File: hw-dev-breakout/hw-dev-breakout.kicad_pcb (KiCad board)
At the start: 2 copper layers, 70 x 57.5 mm, 5 parts, among them J1 CN7, J2 CN10

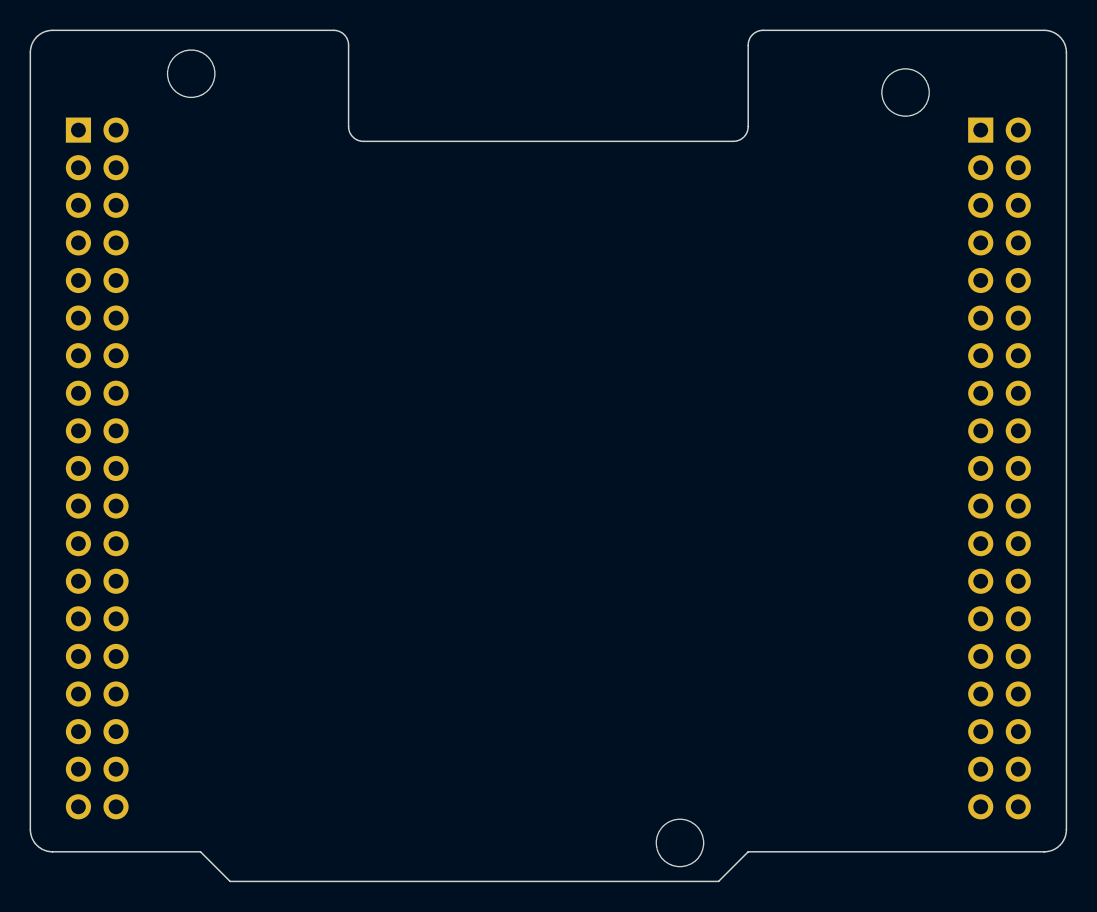
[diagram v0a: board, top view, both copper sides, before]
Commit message: pcb: Move the Nucleo outline onto a comment layout
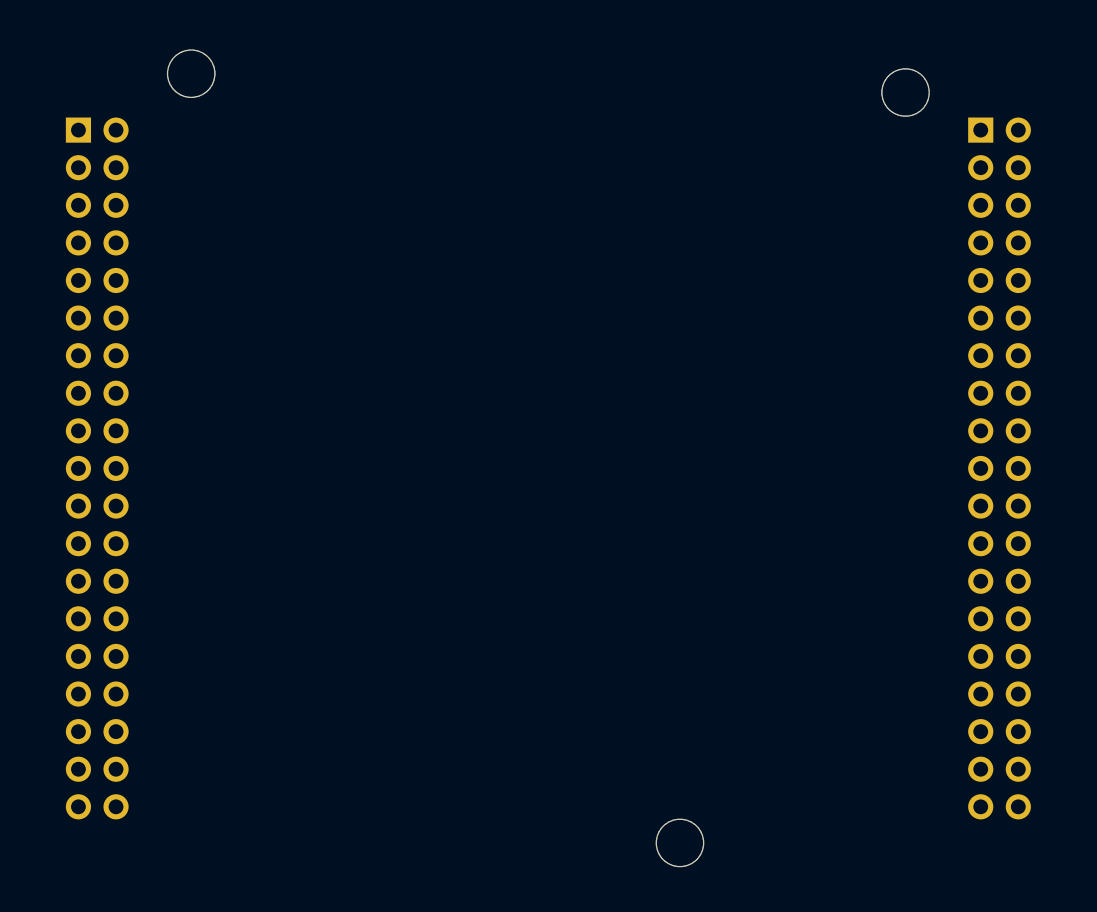
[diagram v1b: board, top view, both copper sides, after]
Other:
- board outline removed
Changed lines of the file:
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@@
 			(type solid)
 		)
-		(layer "Edge.Cuts")
+		(layer "Cmts.User")
 	)
 	(gr_line
@@
 			(type solid)
 		)
-		(layer "Edge.Cuts")
+		(layer "Cmts.User")
 	)
 	(gr_arc
@@
 			(type solid)
 		)
-		(layer "Edge.Cuts")
+		(layer "Cmts.User")
 	)
 	(gr_line
@@
 			(type solid)
 		)
-		(layer "Edge.Cuts")
+		(layer "Cmts.User")
 	)
 	(gr_arc
@@
 			(type solid)
 		)
-		(layer "Edge.Cuts")
+		(layer "Cmts.User")
 	)
 	(gr_arc
@@
 			(type solid)
 		)
-		(layer "Edge.Cuts")
+		(layer "Cmts.User")
 	)
 	(gr_arc
@@
 			(type solid)
 		)
-		(layer "Edge.Cuts")
+		(layer "Cmts.User")
 	)
 	(gr_arc
@@
 			(type solid)
 		)
-		(layer "Edge.Cuts")
+		(layer "Cmts.User")
 	)
 	(gr_line
@@
 			(type solid)
 		)
-		(layer "Edge.Cuts")
+		(layer "Cmts.User")
 	)
 	(gr_arc
@@
 			(type solid)
 		)
-		(layer "Edge.Cuts")
+		(layer "Cmts.User")
 	)
 	(gr_line
@@
 			(type solid)
 		)
-		(layer "Edge.Cuts")
+		(layer "Cmts.User")
 	)
 	(gr_line
@@
 			(type solid)
 		)
-		(layer "Edge.Cuts")
+		(layer "Cmts.User")
 	)
 	(gr_arc
@@
 			(type solid)
 		)
-		(layer "Edge.Cuts")
+		(layer "Cmts.User")
 	)
 	(gr_line
@@
 			(type solid)
 		)
-		(layer "Edge.Cuts")
+		(layer "Cmts.User")
 	)
 	(gr_arc
@@
 			(type solid)
 		)
-		(layer "Edge.Cuts")
+		(layer "Cmts.User")
 	)
 	(gr_line
@@
 			(type solid)
 		)
-		(layer "Edge.Cuts")
+		(layer "Cmts.User")
 	)
 	(gr_line
@@
 			(type solid)
 		)
-		(layer "Edge.Cuts")
+		(layer "Cmts.User")
 	)
 	(gr_line
@@
 			(type solid)
 		)
-		(layer "Edge.Cuts")
+		(layer "Cmts.User")
 	)
 	(gr_line
@@
 			(type solid)
 		)
-		(layer "Edge.Cuts")
+		(layer "Cmts.User")
 	)
 	(gr_line
@@
 			(type solid)
 		)
-		(layer "Edge.Cuts")
+		(layer "Cmts.User")
 	)
 )

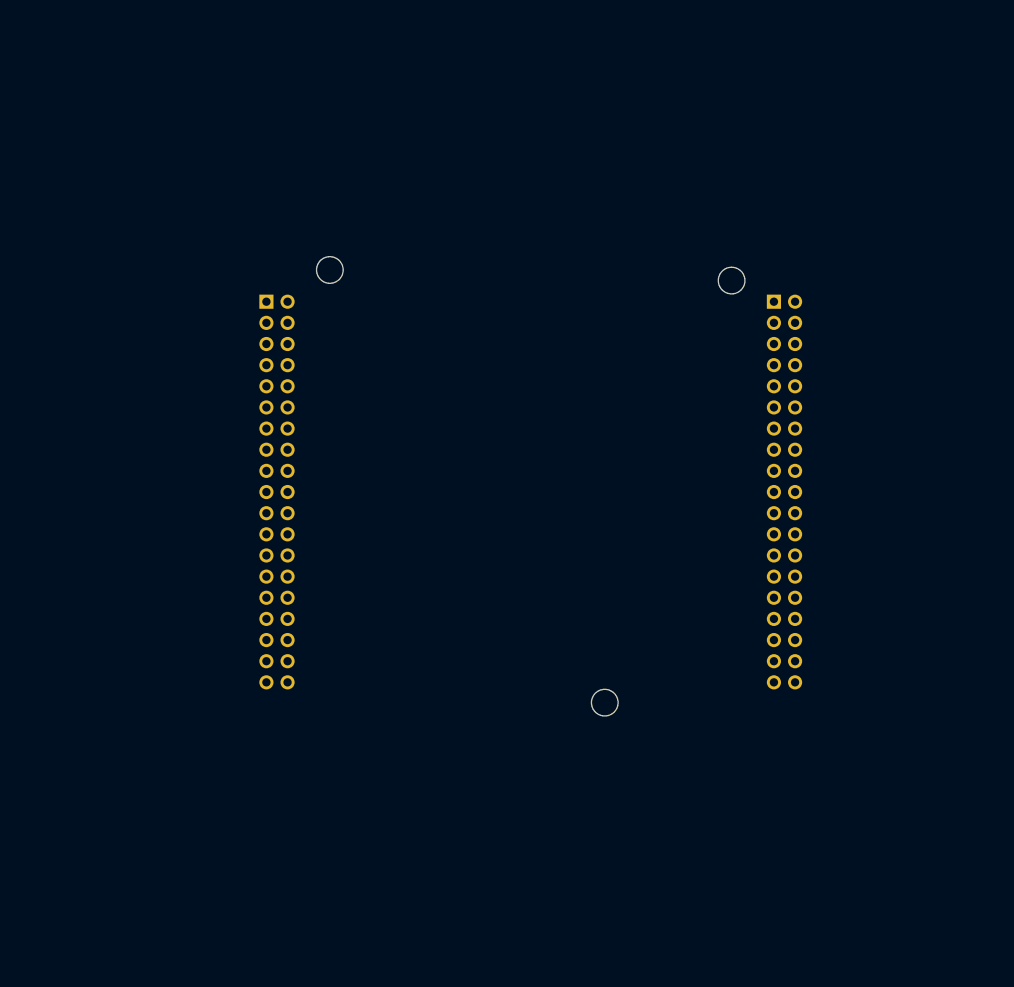
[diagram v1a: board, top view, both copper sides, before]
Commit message: pcb: Initial components placed
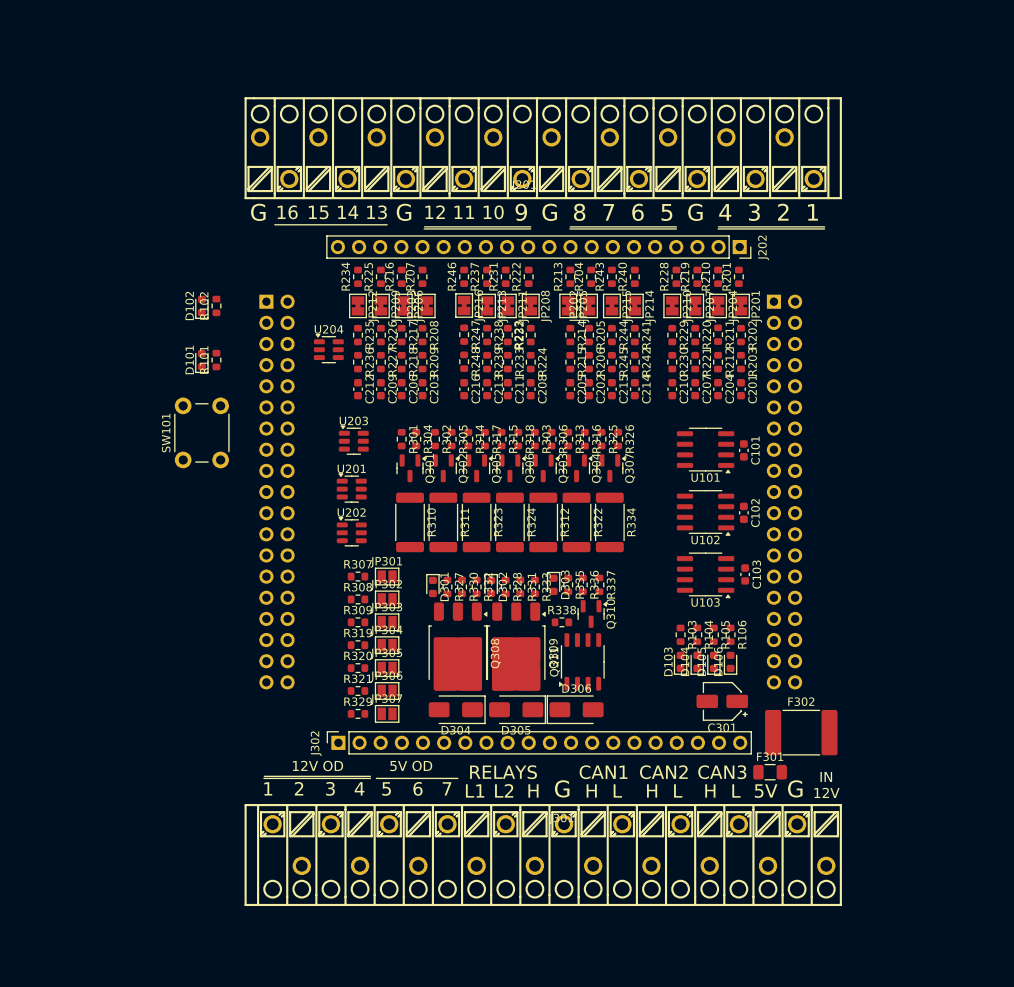
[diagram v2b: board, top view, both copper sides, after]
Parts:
- removed H1, H2, H3: MountingHole, MountingHole:MountingHole_3.2mm_M3
- added C101: 100nF, Capacitor_SMD:C_0603_1608Metric, F.Cu at (162.1, 80.1)
- added C102: 100nF, Capacitor_SMD:C_0603_1608Metric, F.Cu at (162.1, 87.6)
- added C103: 100nF, Capacitor_SMD:C_0603_1608Metric, F.Cu at (162.2, 95.0)
- added C201: DNP, Capacitor_SMD:C_0603_1608Metric, F.Cu at (161.8, 72.8)
- added C202: DNP, Capacitor_SMD:C_0603_1608Metric, F.Cu at (143.5, 72.8)
- added C203: DNP, Capacitor_SMD:C_0603_1608Metric, F.Cu at (123.5, 72.8)
- added C204: DNP, Capacitor_SMD:C_0603_1608Metric, F.Cu at (159.0, 72.8)
- added C205: DNP, Capacitor_SMD:C_0603_1608Metric, F.Cu at (141.2, 72.8)
- added C206: DNP, Capacitor_SMD:C_0603_1608Metric, F.Cu at (121.0, 72.8)
- added C207: DNP, Capacitor_SMD:C_0603_1608Metric, F.Cu at (156.2, 72.8)
- added C208: DNP, Capacitor_SMD:C_0603_1608Metric, F.Cu at (136.5, 72.8)
- added C209: DNP, Capacitor_SMD:C_0603_1608Metric, F.Cu at (118.5, 72.8)
- added C210: DNP, Capacitor_SMD:C_0603_1608Metric, F.Cu at (153.5, 72.8)
- added C211: DNP, Capacitor_SMD:C_0603_1608Metric, F.Cu at (133.8, 72.8)
- added C212: DNP, Capacitor_SMD:C_0603_1608Metric, F.Cu at (115.8, 72.8)
- added C213: DNP, Capacitor_SMD:C_0603_1608Metric, F.Cu at (131.2, 72.8)
- added C214: DNP, Capacitor_SMD:C_0603_1608Metric, F.Cu at (149.0, 72.8)
- added C215: DNP, Capacitor_SMD:C_0603_1608Metric, F.Cu at (146.2, 72.8)
- added C216: DNP, Capacitor_SMD:C_0603_1608Metric, F.Cu at (128.5, 72.8)
- added C301: 10uF 25V, Capacitor_SMD:CP_Elec_4x4.5, F.Cu at (159.5, 110.2)
- added D101: RED, LED_SMD:LED_0603_1608Metric, F.Cu at (97.0, 69.2)
- added D102: RED, LED_SMD:LED_0603_1608Metric, F.Cu at (97.0, 62.8)
- added D103: GREEN, LED_SMD:LED_0603_1608Metric, F.Cu at (154.5, 105.5)
- added D104: GREEN, LED_SMD:LED_0603_1608Metric, F.Cu at (156.5, 105.5)
- added D105: GREEN, LED_SMD:LED_0603_1608Metric, F.Cu at (158.5, 105.5)
- added D106: GREEN, LED_SMD:LED_0603_1608Metric, F.Cu at (160.5, 105.5)
- added D301: ORANGE, LED_SMD:LED_0603_1608Metric, F.Cu at (124.8, 96.5)
- added D302: ORANGE, LED_SMD:LED_0603_1608Metric, F.Cu at (131.8, 96.5)
- added D303: ORANGE, LED_SMD:LED_0603_1608Metric, F.Cu at (139.2, 96.2)
- added D304: SS54, Diode_SMD:D_SMA, F.Cu at (127.5, 111.2)
- added D305: SS54, Diode_SMD:D_SMA, F.Cu at (134.8, 111.2)
- added D306: SS54, Diode_SMD:D_SMA, F.Cu at (142.0, 111.2)
- added F301: 12H1100C 1A, Fuse:Fuse_1206_3216Metric, F.Cu at (165.2, 118.8)
- added F302: LSMD500, Fuse:Fuse_2920_7451Metric, F.Cu at (169.0, 114.0)
- added J201: WAGO 250-220, hw-dev-breakout:CONN-TH_250-220, F.Cu at (137.2, 45.0)
- added J202: Conn_01x16, Connector_PinSocket_2.54mm:PinSocket_1x20_P2.54mm_Vertical, F.Cu at (161.6, 55.7)
- added J301: WAGO 250-220, hw-dev-breakout:CONN-TH_250-220, F.Cu at (138.8, 127.5)
- added J302: Conn_01x20, Connector_PinSocket_2.54mm:PinSocket_1x20_P2.54mm_Vertical, F.Cu at (113.4, 115.2)
- added JP201: SolderJumper_2_Bridged, Jumper:SolderJumper-2_P1.3mm_Bridged_Pad1.0x1.5mm, F.Cu at (161.8, 62.8)
- added JP202: SolderJumper_2_Bridged, Jumper:SolderJumper-2_P1.3mm_Bridged_Pad1.0x1.5mm, F.Cu at (143.5, 62.8)
- added JP203: SolderJumper_2_Bridged, Jumper:SolderJumper-2_P1.3mm_Bridged_Pad1.0x1.5mm, F.Cu at (124.0, 62.8)
- added JP204: SolderJumper_2_Bridged, Jumper:SolderJumper-2_P1.3mm_Bridged_Pad1.0x1.5mm, F.Cu at (159.0, 62.8)
- added JP205: SolderJumper_2_Bridged, Jumper:SolderJumper-2_P1.3mm_Bridged_Pad1.0x1.5mm, F.Cu at (141.0, 62.8)
- added JP206: SolderJumper_2_Bridged, Jumper:SolderJumper-2_P1.3mm_Bridged_Pad1.0x1.5mm, F.Cu at (121.2, 62.8)
- added JP207: SolderJumper_2_Bridged, Jumper:SolderJumper-2_P1.3mm_Bridged_Pad1.0x1.5mm, F.Cu at (156.2, 62.8)
- added JP208: SolderJumper_2_Bridged, Jumper:SolderJumper-2_P1.3mm_Bridged_Pad1.0x1.5mm, F.Cu at (136.5, 62.8)
- added JP209: SolderJumper_2_Bridged, Jumper:SolderJumper-2_P1.3mm_Bridged_Pad1.0x1.5mm, F.Cu at (118.5, 62.8)
- added JP210: SolderJumper_2_Bridged, Jumper:SolderJumper-2_P1.3mm_Bridged_Pad1.0x1.5mm, F.Cu at (153.5, 62.8)
- added JP211: SolderJumper_2_Bridged, Jumper:SolderJumper-2_P1.3mm_Bridged_Pad1.0x1.5mm, F.Cu at (133.8, 62.8)
- added JP212: SolderJumper_2_Bridged, Jumper:SolderJumper-2_P1.3mm_Bridged_Pad1.0x1.5mm, F.Cu at (115.8, 62.8)
- added JP213: SolderJumper_2_Bridged, Jumper:SolderJumper-2_P1.3mm_Bridged_Pad1.0x1.5mm, F.Cu at (131.2, 62.8)
- added JP214: SolderJumper_2_Bridged, Jumper:SolderJumper-2_P1.3mm_Bridged_Pad1.0x1.5mm, F.Cu at (149.0, 62.8)
- added JP215: SolderJumper_2_Bridged, Jumper:SolderJumper-2_P1.3mm_Bridged_Pad1.0x1.5mm, F.Cu at (146.2, 62.8)
- added JP216: SolderJumper_2_Bridged, Jumper:SolderJumper-2_P1.3mm_Bridged_Pad1.0x1.5mm, F.Cu at (128.5, 62.7)
- added JP301: SolderJumper_2_Open, Jumper:SolderJumper-2_P1.3mm_Open_Pad1.0x1.5mm, F.Cu at (119.2, 95.2)
- added JP302: SolderJumper_2_Open, Jumper:SolderJumper-2_P1.3mm_Open_Pad1.0x1.5mm, F.Cu at (119.2, 98.0)
- added JP303: SolderJumper_2_Open, Jumper:SolderJumper-2_P1.3mm_Open_Pad1.0x1.5mm, F.Cu at (119.2, 100.8)
- added JP304: SolderJumper_2_Open, Jumper:SolderJumper-2_P1.3mm_Open_Pad1.0x1.5mm, F.Cu at (119.2, 103.5)
- added JP305: SolderJumper_2_Open, Jumper:SolderJumper-2_P1.3mm_Open_Pad1.0x1.5mm, F.Cu at (119.2, 106.2)
- added JP306: SolderJumper_2_Open, Jumper:SolderJumper-2_P1.3mm_Open_Pad1.0x1.5mm, F.Cu at (119.2, 109.0)
- added JP307: SolderJumper_2_Open, Jumper:SolderJumper-2_P1.3mm_Open_Pad1.0x1.5mm, F.Cu at (119.2, 111.8)
- added Q301: 2N7002, Package_TO_SOT_SMD:SOT-23, F.Cu at (122.0, 82.2)
- added Q302: 2N7002, Package_TO_SOT_SMD:SOT-23, F.Cu at (126.0, 82.2)
- added Q303: 2N7002, Package_TO_SOT_SMD:SOT-23, F.Cu at (138.0, 82.2)
- added Q304: 2N7002, Package_TO_SOT_SMD:SOT-23, F.Cu at (142.0, 82.2)
- added Q305: 2N7002, Package_TO_SOT_SMD:SOT-23, F.Cu at (130.0, 82.2)
- added Q306: 2N7002, Package_TO_SOT_SMD:SOT-23, F.Cu at (134.0, 82.2)
- added Q307: 2N7002, Package_TO_SOT_SMD:SOT-23, F.Cu at (146.0, 82.2)
- added Q308: HL 20N04, Package_TO_SOT_SMD:TO-252-3_TabPin2, F.Cu at (127.8, 104.5)
- added Q309: HL 20N04, Package_TO_SOT_SMD:TO-252-3_TabPin2, F.Cu at (134.8, 104.5)
- added Q310: 2N7002, Package_TO_SOT_SMD:SOT-23, F.Cu at (143.8, 99.8)
- added Q311: Q_PMOS_HL_4485, Package_SO:SOP-8_3.9x4.9mm_P1.27mm, F.Cu at (142.8, 105.5)
- added R101: 330R, Resistor_SMD:R_0603_1608Metric, F.Cu at (98.8, 69.2)
- added R102: 10K, Resistor_SMD:R_0603_1608Metric, F.Cu at (98.8, 62.8)
- added R103: 330R, Resistor_SMD:R_0603_1608Metric, F.Cu at (154.5, 102.2)
- added R104: 330R, Resistor_SMD:R_0603_1608Metric, F.Cu at (156.5, 102.2)
- added R105: 330R, Resistor_SMD:R_0603_1608Metric, F.Cu at (158.5, 102.2)
- added R106: 330R, Resistor_SMD:R_0603_1608Metric, F.Cu at (160.5, 102.2)
- added R201: 1K, Resistor_SMD:R_0603_1608Metric, F.Cu at (161.5, 59.2)
- added R202: 33K, Resistor_SMD:R_0603_1608Metric, F.Cu at (161.8, 66.2)
- added R203: 10K, Resistor_SMD:R_0603_1608Metric, F.Cu at (161.8, 69.5)
- added R204: 1K, Resistor_SMD:R_0603_1608Metric, F.Cu at (143.8, 59.2)
- added R205: 33K, Resistor_SMD:R_0603_1608Metric, F.Cu at (143.5, 66.2)
- added R206: 10K, Resistor_SMD:R_0603_1608Metric, F.Cu at (143.5, 69.5)
- added R207: 1K, Resistor_SMD:R_0603_1608Metric, F.Cu at (123.5, 59.2)
- added R208: 6.8K, Resistor_SMD:R_0603_1608Metric, F.Cu at (123.5, 66.2)
- added R209: 10K, Resistor_SMD:R_0603_1608Metric, F.Cu at (123.5, 69.5)
- added R210: 1K, Resistor_SMD:R_0603_1608Metric, F.Cu at (159.0, 59.2)
- added R211: 33K, Resistor_SMD:R_0603_1608Metric, F.Cu at (159.0, 66.2)
- added R212: 10K, Resistor_SMD:R_0603_1608Metric, F.Cu at (159.0, 69.5)
- added R213: 1K, Resistor_SMD:R_0603_1608Metric, F.Cu at (141.2, 59.2)
- added R214: 33K, Resistor_SMD:R_0603_1608Metric, F.Cu at (141.2, 66.2)
- added R215: 10K, Resistor_SMD:R_0603_1608Metric, F.Cu at (141.2, 69.5)
- added R216: 1K, Resistor_SMD:R_0603_1608Metric, F.Cu at (121.0, 59.2)
- added R217: 6.8K, Resistor_SMD:R_0603_1608Metric, F.Cu at (121.0, 66.2)
- added R218: 10K, Resistor_SMD:R_0603_1608Metric, F.Cu at (121.0, 69.5)
- added R219: 1K, Resistor_SMD:R_0603_1608Metric, F.Cu at (156.5, 59.2)
- added R220: 33K, Resistor_SMD:R_0603_1608Metric, F.Cu at (156.2, 66.2)
- added R221: 10K, Resistor_SMD:R_0603_1608Metric, F.Cu at (156.2, 69.5)
- added R222: 1K, Resistor_SMD:R_0603_1608Metric, F.Cu at (136.2, 59.2)
- added R223: 33K, Resistor_SMD:R_0603_1608Metric, F.Cu at (136.5, 66.2)
- added R224: 10K, Resistor_SMD:R_0603_1608Metric, F.Cu at (136.5, 69.5)
- added R225: 1K, Resistor_SMD:R_0603_1608Metric, F.Cu at (118.5, 59.2)
- added R226: 6.8K, Resistor_SMD:R_0603_1608Metric, F.Cu at (118.5, 66.2)
- added R227: 10K, Resistor_SMD:R_0603_1608Metric, F.Cu at (118.5, 69.5)
- added R228: 1K, Resistor_SMD:R_0603_1608Metric, F.Cu at (154.0, 59.2)
- added R229: 33K, Resistor_SMD:R_0603_1608Metric, F.Cu at (153.5, 66.2)
- added R230: 10K, Resistor_SMD:R_0603_1608Metric, F.Cu at (153.5, 69.5)
- added R231: 1K, Resistor_SMD:R_0603_1608Metric, F.Cu at (133.5, 59.2)
- added R232: 33K, Resistor_SMD:R_0603_1608Metric, F.Cu at (133.8, 66.2)
- added R233: 10K, Resistor_SMD:R_0603_1608Metric, F.Cu at (133.8, 69.5)
- added R234: 1K, Resistor_SMD:R_0603_1608Metric, F.Cu at (115.8, 59.2)
- added R235: 6.8K, Resistor_SMD:R_0603_1608Metric, F.Cu at (115.8, 66.2)
- added R236: 10K, Resistor_SMD:R_0603_1608Metric, F.Cu at (115.8, 69.5)
- added R237: 1K, Resistor_SMD:R_0603_1608Metric, F.Cu at (131.2, 59.2)
- added R238: 33K, Resistor_SMD:R_0603_1608Metric, F.Cu at (131.2, 66.2)
- added R239: 10K, Resistor_SMD:R_0603_1608Metric, F.Cu at (131.2, 69.5)
- added R240: 1K, Resistor_SMD:R_0603_1608Metric, F.Cu at (149.0, 59.2)
- added R241: 33K, Resistor_SMD:R_0603_1608Metric, F.Cu at (149.0, 66.2)
- added R242: 10K, Resistor_SMD:R_0603_1608Metric, F.Cu at (149.0, 69.5)
- added R243: 1K, Resistor_SMD:R_0603_1608Metric, F.Cu at (146.2, 59.2)
- added R244: 33K, Resistor_SMD:R_0603_1608Metric, F.Cu at (146.2, 66.2)
- added R245: 10K, Resistor_SMD:R_0603_1608Metric, F.Cu at (146.2, 69.5)
- added R246: 1K, Resistor_SMD:R_0603_1608Metric, F.Cu at (128.5, 59.2)
- added R247: 33K, Resistor_SMD:R_0603_1608Metric, F.Cu at (128.5, 66.2)
- added R248: 10K, Resistor_SMD:R_0603_1608Metric, F.Cu at (128.5, 69.5)
- added R301: 10K, Resistor_SMD:R_0603_1608Metric, F.Cu at (121.0, 78.8)
- added R302: 10K, Resistor_SMD:R_0603_1608Metric, F.Cu at (125.0, 78.8)
- added R303: 10K, Resistor_SMD:R_0603_1608Metric, F.Cu at (137.0, 78.8)
- added R304: 33R, Resistor_SMD:R_0603_1608Metric, F.Cu at (122.8, 78.8)
- added R305: 33R, Resistor_SMD:R_0603_1608Metric, F.Cu at (127.0, 78.8)
- added R306: 33R, Resistor_SMD:R_0603_1608Metric, F.Cu at (139.0, 78.8)
- added R307: 1K, Resistor_SMD:R_0603_1608Metric, F.Cu at (115.8, 95.2)
- added R308: 1K, Resistor_SMD:R_0603_1608Metric, F.Cu at (115.8, 98.0)
- added R309: 1K, Resistor_SMD:R_0603_1608Metric, F.Cu at (115.8, 100.8)
- added R310: 100R 2W, Resistor_SMD:R_2512_6332Metric, F.Cu at (122.0, 88.8)
- added R311: 100R 2W, Resistor_SMD:R_2512_6332Metric, F.Cu at (126.0, 88.8)
- added R312: 100R 2W, Resistor_SMD:R_2512_6332Metric, F.Cu at (138.0, 88.8)
- added R313: 10K, Resistor_SMD:R_0603_1608Metric, F.Cu at (141.0, 78.8)
- added R314: 10K, Resistor_SMD:R_0603_1608Metric, F.Cu at (129.0, 78.8)
- added R315: 10K, Resistor_SMD:R_0603_1608Metric, F.Cu at (133.0, 78.8)
- added R316: 33R, Resistor_SMD:R_0603_1608Metric, F.Cu at (143.0, 78.8)
- added R317: 33R, Resistor_SMD:R_0603_1608Metric, F.Cu at (131.0, 78.8)
- added R318: 33R, Resistor_SMD:R_0603_1608Metric, F.Cu at (135.0, 78.8)
- added R319: 1K, Resistor_SMD:R_0603_1608Metric, F.Cu at (115.8, 103.5)
- added R320: 1K, Resistor_SMD:R_0603_1608Metric, F.Cu at (115.8, 106.2)
- added R321: 1K, Resistor_SMD:R_0603_1608Metric, F.Cu at (115.8, 109.0)
- added R322: 100R 2W, Resistor_SMD:R_2512_6332Metric, F.Cu at (142.0, 88.8)
- added R323: 100R 2W, Resistor_SMD:R_2512_6332Metric, F.Cu at (130.0, 88.8)
- added R324: 100R 2W, Resistor_SMD:R_2512_6332Metric, F.Cu at (134.0, 88.8)
- added R325: 10K, Resistor_SMD:R_0603_1608Metric, F.Cu at (145.0, 78.8)
- added R326: 33R, Resistor_SMD:R_0603_1608Metric, F.Cu at (147.0, 78.8)
- added R327: 330R, Resistor_SMD:R_0603_1608Metric, F.Cu at (126.5, 96.5)
- added R328: 330R, Resistor_SMD:R_0603_1608Metric, F.Cu at (133.5, 96.5)
- added R329: 1K, Resistor_SMD:R_0603_1608Metric, F.Cu at (115.8, 111.8)
- added R330: 10K, Resistor_SMD:R_0603_1608Metric, F.Cu at (128.2, 96.5)
- added R331: 10K, Resistor_SMD:R_0603_1608Metric, F.Cu at (135.2, 96.5)
- added R332: 33R, Resistor_SMD:R_0603_1608Metric, F.Cu at (130.0, 96.5)
- added R333: 33R, Resistor_SMD:R_0603_1608Metric, F.Cu at (137.0, 96.5)
- added R334: 100R 2W, Resistor_SMD:R_2512_6332Metric, F.Cu at (146.0, 88.8)
- added R335: 330R, Resistor_SMD:R_0603_1608Metric, F.Cu at (141.0, 96.2)
- added R336: 10K, Resistor_SMD:R_0603_1608Metric, F.Cu at (142.8, 96.2)
- added R337: 33R, Resistor_SMD:R_0603_1608Metric, F.Cu at (144.8, 96.2)
- added R338: 1K, Resistor_SMD:R_0603_1608Metric, F.Cu at (140.2, 100.8)
- added SW101: SW_Push, Button_Switch_THT:SW_PUSH_6mm_H8mm, F.Cu at (94.8, 81.2)
- added U101: TCAN332, Package_SO:SOIC-8_3.9x4.9mm_P1.27mm, F.Cu at (157.5, 80.0)
- added U102: TCAN332, Package_SO:SOIC-8_3.9x4.9mm_P1.27mm, F.Cu at (157.5, 87.5)
- added U103: TCAN332, Package_SO:SOIC-8_3.9x4.9mm_P1.27mm, F.Cu at (157.5, 95.0)
- added U201: CM1293A-04SO, Package_TO_SOT_SMD:SOT-23-6, F.Cu at (115.0, 84.8)
- added U202: CM1293A-04SO, Package_TO_SOT_SMD:SOT-23-6, F.Cu at (115.0, 90.0)
- added U203: CM1293A-04SO, Package_TO_SOT_SMD:SOT-23-6, F.Cu at (115.2, 79.0)
- added U204: CM1293A-04SO, Package_TO_SOT_SMD:SOT-23-6, F.Cu at (112.2, 68.0)
- renumbered J1 to J101, J2 to J102
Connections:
- J101 pad 1: unconnected-(J1-Pad1) -> /IN14
- J101 pad 16: +3V3 -> +3.3V
- J101 pad 2: unconnected-(J1-Pad2) -> /IN13
- J101 pad 28: unconnected-(J1-Pad28) -> /IN1
- J101 pad 3: unconnected-(J1-Pad3) -> /IN15
- J101 pad 30: unconnected-(J1-Pad30) -> /IN2
- J101 pad 32: unconnected-(J1-Pad32) -> /IN3
- J101 pad 33: +BATT -> unconnected-(J101-Pin_33-Pad33)
- J101 pad 34: unconnected-(J1-Pad34) -> /IN4
- J101 pad 35: unconnected-(J1-Pad35) -> /IN7
- J101 pad 36: unconnected-(J1-Pad36) -> /IN5
- J101 pad 37: unconnected-(J1-Pad37) -> /IN8
- J101 pad 38: unconnected-(J1-Pad38) -> /IN6
- J101 pad 4: unconnected-(J1-Pad4) -> /IN16
- J101 pad 5: VDD -> unconnected-(J101-Pin_5-Pad5)
- J102 pad 1: unconnected-(J2-Pad1) -> /IN12
- J102 pad 11: unconnected-(J2-Pad11) -> /OUT3
- J102 pad 12: unconnected-(J2-Pad12) -> /FDCAN1_TX
- J102 pad 13: unconnected-(J2-Pad13) -> /OUT4
- J102 pad 14: unconnected-(J2-Pad14) -> /FDCAN1_RX
- J102 pad 15: unconnected-(J2-Pad15) -> /OUT5
- J102 pad 16: unconnected-(J2-Pad16) -> /FDCAN2_RX
- J102 pad 17: unconnected-(J2-Pad17) -> /COIL_L1
- J102 pad 18: unconnected-(J2-Pad18) -> /LED4
- J102 pad 19: unconnected-(J2-Pad19) -> /IN11
- J102 pad 2: unconnected-(J2-Pad2) -> /LED1
- J102 pad 21: unconnected-(J2-Pad21) -> /OUT7
- J102 pad 23: unconnected-(J2-Pad23) -> /OUT6
- J102 pad 25: unconnected-(J2-Pad25) -> /COIL_L2
- J102 pad 27: unconnected-(J2-Pad27) -> /FDCAN3_TX
- J102 pad 29: unconnected-(J2-Pad29) -> /COIL_H
- J102 pad 3: unconnected-(J2-Pad3) -> /OUT1
- J102 pad 30: unconnected-(J2-Pad30) -> /FDCAN2_TX
- J102 pad 31: unconnected-(J2-Pad31) -> /FDCAN3_RX
- J102 pad 32: GNDA -> unconnected-(J102-Pin_32-Pad32)
- J102 pad 34: unconnected-(J2-Pad34) -> /IN9
- J102 pad 37: unconnected-(J2-Pad37) -> /IN10
- J102 pad 4: unconnected-(J2-Pad4) -> /LED2
- J102 pad 5: unconnected-(J2-Pad5) -> /OUT2
- J102 pad 6: unconnected-(J2-Pad6) -> /LED3
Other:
- copper layers 2 -> 4
- board text added: "1"
- board text added: "10"
- board text added: "11"
- board text added: "12"
- board text added: "12V OD"
- board text added: "13"
- board text added: "14"
- board text added: "15"
- board text added: "16"
- board text added: "2"
- board text added: "3"
- board text added: "4"
- board text added: "5"
- board text added: "5V"
- board text added: "5V OD"
- board text added: "6"
- board text added: "7"
- board text added: "8"
- board text added: "9"
- board text added: "CAN1"
- board text added: "CAN2"
- board text added: "CAN3"
- board text added: "G"
- board text added: "H"
- board text added: "IN 12V"
- board text added: "L"
- board text added: "L1"
- board text added: "L2"
- board text added: "RELAYS"

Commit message: pcb: Partially routed
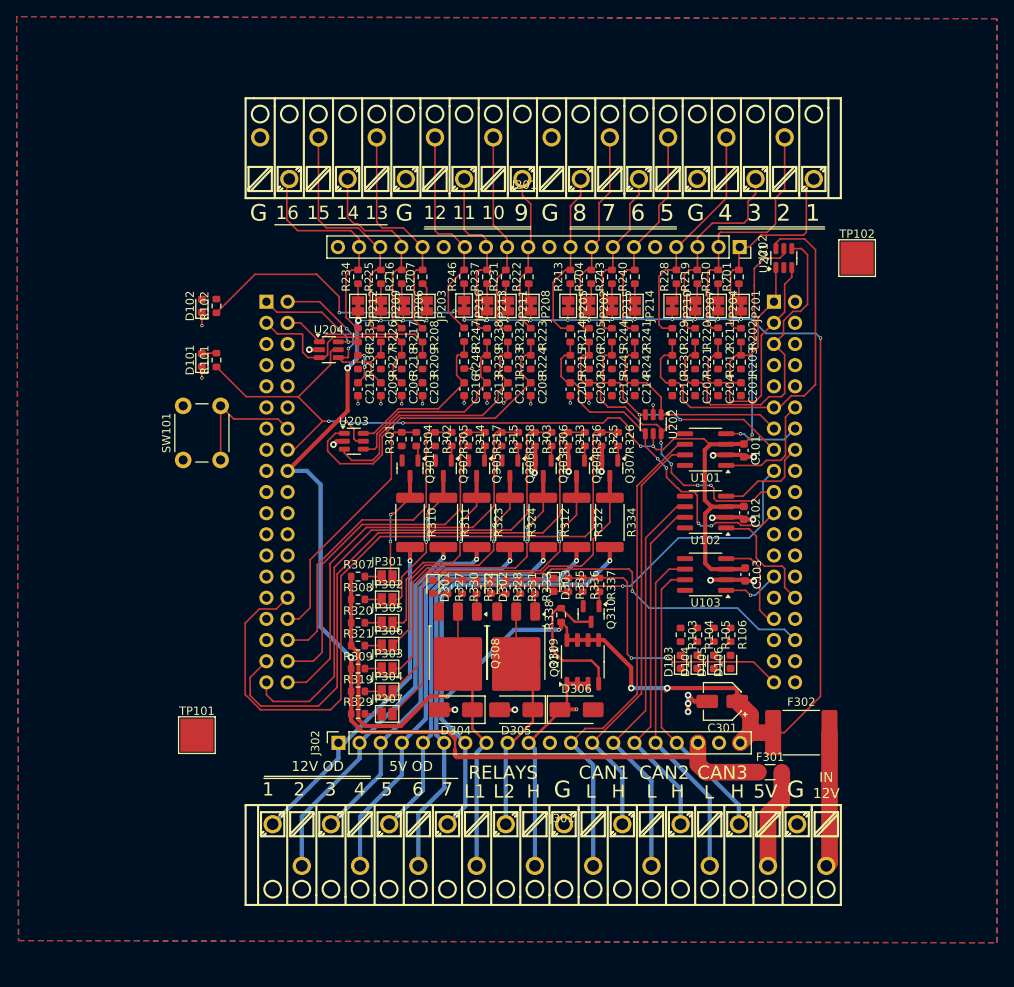
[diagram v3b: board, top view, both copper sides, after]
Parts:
- added TP101: TestPoint, TestPoint:TestPoint_Pad_4.0x4.0mm, F.Cu at (96.4, 114.3)
- added TP102: TestPoint, TestPoint:TestPoint_Pad_4.0x4.0mm, F.Cu at (175.7, 57.0)
- moved U201 58.9 mm to (166.9, 57.0), turned to 90 degrees
- moved U202 38.5 mm to (151.2, 77.0), turned to -90 degrees
- moved JP303 5.55 mm to (119.2, 106.3)
- moved JP304 5.55 mm to (119.2, 109.0)
- moved R309 5.55 mm to (115.8, 106.3)
- moved R319 5.55 mm to (115.8, 109.0)
- moved JP305 5.45 mm to (119.2, 100.8)
- moved JP306 5.45 mm to (119.2, 103.5)
- moved R320 5.45 mm to (115.8, 100.8)
- moved R321 5.45 mm to (115.8, 103.5)
- moved R338 0.88 mm to (140.2, 99.9), turned to 90 degrees
- turned JP202 to -90 degrees
- turned JP203 to -90 degrees
- turned R223 to -90 degrees
- turned R301 to 90 degrees
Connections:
- J101 pad 1: /IN14 -> /IN16
- J101 pad 17: unconnected-(J101-Pin_17-Pad17) -> /IN12
- J101 pad 2: /IN13 -> /IN15
- J101 pad 21: unconnected-(J101-Pin_21-Pad21) -> /IN11
- J101 pad 28: /IN1 -> /IN10
- J101 pad 3: /IN15 -> /IN14
- J101 pad 30: /IN2 -> /OUT7
- J101 pad 32: /IN3 -> /OUT1
- J101 pad 34: /IN4 -> /OUT2
- J101 pad 35: /IN7 -> /OUT6
- J101 pad 36: /IN5 -> /OUT3
- J101 pad 37: /IN8 -> /OUT5
- J101 pad 38: /IN6 -> /OUT4
- J101 pad 4: /IN16 -> /IN13
- J102 pad 1: /IN12 -> /IN1
- J102 pad 11: /OUT3 -> /IN4
- J102 pad 13: /OUT4 -> /IN5
- J102 pad 15: /OUT5 -> /IN6
- J102 pad 19: /IN11 -> /IN7
- J102 pad 21: /OUT7 -> /IN8
- J102 pad 23: /OUT6 -> /IN9
- J102 pad 25: /COIL_L2 -> unconnected-(J102-Pin_25-Pad25)
- J102 pad 29: /COIL_H -> unconnected-(J102-Pin_29-Pad29)
- J102 pad 3: /OUT1 -> /IN2
- J102 pad 34: /IN9 -> /COIL_L2
- J102 pad 37: /IN10 -> /COIL_H
- J102 pad 5: /OUT2 -> /IN3
- J301 pad 12: /CAN1_H -> /CAN1_L
- J301 pad 13: /CAN1_L -> /CAN1_H
- J301 pad 14: /CAN2_H -> /CAN2_L
- J301 pad 15: /CAN2_L -> /CAN2_H
- J301 pad 16: /CAN3_H -> /CAN3_L
- J301 pad 17: /CAN3_L -> /CAN3_H
- J302 pad 12: /CAN1_H -> /CAN1_L
- J302 pad 13: /CAN1_L -> /CAN1_H
- J302 pad 14: /CAN2_H -> /CAN2_L
- J302 pad 15: /CAN2_L -> /CAN2_H
- J302 pad 16: /CAN3_H -> /CAN3_L
- J302 pad 17: /CAN3_L -> /CAN3_H
- U202 pad 4: /IN7 -> /IN8
- U202 pad 6: /IN8 -> /IN7
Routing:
- net +12V: track 0.00 -> 226.7 mm, vias 0 -> 19
- net +3.3V: track 0.00 -> 152.0 mm, vias 0 -> 7
- net +5V: track 0.00 -> 126.7 mm, vias 0 -> 6
- net /OUT7: track 0.00 -> 89.6 mm
- net /OUT6: track 0.00 -> 72.8 mm
- net /OUT5: track 0.00 -> 62.7 mm
- net /CAN1_L: track 0.00 -> 59.1 mm
- net /Outputs/5V_OUT6: track 0.00 -> 54.5 mm, vias 0 -> 1
- net /Outputs/5V_OUT7: track 0.00 -> 53.0 mm, vias 0 -> 1
- net /OUT4: track 0.00 -> 51.9 mm
- net /CAN1_H: track 0.00 -> 51.4 mm
- net GND: track 0.00 -> 50.4 mm, vias 0 -> 30
- net /IN4: track 0.00 -> 49.9 mm
- net /Outputs/12V_OUT4: track 0.00 -> 49.6 mm, vias 0 -> 1
- net Net-(JP307-B): track 0.00 -> 49.5 mm
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- added copper zone on B.Cu, net GND
- added copper zone on F.Cu, net GND
- added copper zone on In1.Cu, net GND
